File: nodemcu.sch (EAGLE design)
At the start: 6 parts

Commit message: uprava desky
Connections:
- new net N$6: U$1.VIN
- net +3V3: now also U$1.3V3@2; no longer U$1.VIN
- net GND: now also U$1.GND@3; no longer U$1.GND@1
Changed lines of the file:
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@@
 <?xml version="1.0" encoding="utf-8"?>
 <!DOCTYPE eagle SYSTEM "eagle.dtd">
-<eagle version="7.7.0">
+<eagle version="7.3.0">
 <drawing>
 <settings>
@@
 <segment>
 <pinref part="+3V1" gate="G$1" pin="+3V3"/>
-<pinref part="U$1" gate="G$1" pin="VIN"/>
 <wire x1="66.04" y1="43.18" x2="58.42" y2="43.18" width="0.1524" layer="91"/>
-<wire x1="7.62" y1="30.48" x2="5.08" y2="30.48" width="0.1524" layer="91"/>
-<wire x1="5.08" y1="30.48" x2="5.08" y2="17.78" width="0.1524" layer="91"/>
-<wire x1="5.08" y1="17.78" x2="15.24" y2="17.78" width="0.1524" layer="91"/>
 <wire x1="15.24" y1="17.78" x2="66.04" y2="17.78" width="0.1524" layer="91"/>
-<wire x1="66.04" y1="17.78" x2="66.04" y2="43.18" width="0.1524" layer="91"/>
+<wire x1="66.04" y1="17.78" x2="66.04" y2="30.48" width="0.1524" layer="91"/>
 <pinref part="SENSOR" gate="G$1" pin="1"/>
+<wire x1="66.04" y1="30.48" x2="66.04" y2="43.18" width="0.1524" layer="91"/>
 <wire x1="66.04" y1="43.18" x2="81.28" y2="43.18" width="0.1524" layer="91"/>
 <junction x="66.04" y="43.18"/>
 <pinref part="D1" gate="1" pin="C"/>
 <wire x1="15.24" y1="5.08" x2="15.24" y2="7.62" width="0.1524" layer="91"/>
-<junction x="15.24" y="17.78"/>
 <pinref part="SL2" gate="G$1" pin="1"/>
 <wire x1="15.24" y1="7.62" x2="15.24" y2="17.78" width="0.1524" layer="91"/>
@@
 <wire x1="22.86" y1="7.62" x2="22.86" y2="5.08" width="0.1524" layer="91"/>
 <junction x="15.24" y="7.62"/>
+<pinref part="U$1" gate="G$1" pin="3V3@2"/>
+<wire x1="43.18" y1="30.48" x2="66.04" y2="30.48" width="0.1524" layer="91"/>
+<junction x="66.04" y="30.48"/>
 </segment>
 </net>
@@
 <segment>
 <pinref part="GND1" gate="1" pin="GND"/>
-<wire x1="60.96" y1="27.94" x2="60.96" y2="40.64" width="0.1524" layer="91"/>
+<wire x1="60.96" y1="27.94" x2="60.96" y2="33.02" width="0.1524" layer="91"/>
 <pinref part="SENSOR" gate="G$1" pin="2"/>
+<wire x1="60.96" y1="33.02" x2="60.96" y2="40.64" width="0.1524" layer="91"/>
 <wire x1="60.96" y1="40.64" x2="81.28" y2="40.64" width="0.1524" layer="91"/>
 <wire x1="60.96" y1="27.94" x2="45.72" y2="27.94" width="0.1524" layer="91"/>
 <wire x1="45.72" y1="27.94" x2="45.72" y2="15.24" width="0.1524" layer="91"/>
 <junction x="60.96" y="27.94"/>
-<pinref part="U$1" gate="G$1" pin="GND@1"/>
-<wire x1="7.62" y1="33.02" x2="0" y2="33.02" width="0.1524" layer="91"/>
-<wire x1="0" y1="33.02" x2="0" y2="15.24" width="0.1524" layer="91"/>
 <pinref part="X1" gate="-1" pin="KL"/>
-<wire x1="0" y1="15.24" x2="10.16" y2="15.24" width="0.1524" layer="91"/>
 <wire x1="10.16" y1="15.24" x2="10.16" y2="-2.54" width="0.1524" layer="91"/>
 <wire x1="45.72" y1="15.24" x2="10.16" y2="15.24" width="0.1524" layer="91"/>
-<junction x="10.16" y="15.24"/>
+<pinref part="U$1" gate="G$1" pin="GND@3"/>
+<wire x1="43.18" y1="33.02" x2="60.96" y2="33.02" width="0.1524" layer="91"/>
+<junction x="60.96" y="33.02"/>
 </segment>
 </net>
@@
 </segment>
 </net>
+<net name="N$6" class="0">
+<segment>
+<pinref part="U$1" gate="G$1" pin="VIN"/>
+<wire x1="7.62" y1="30.48" x2="5.08" y2="30.48" width="0.1524" layer="91"/>
+</segment>
+</net>

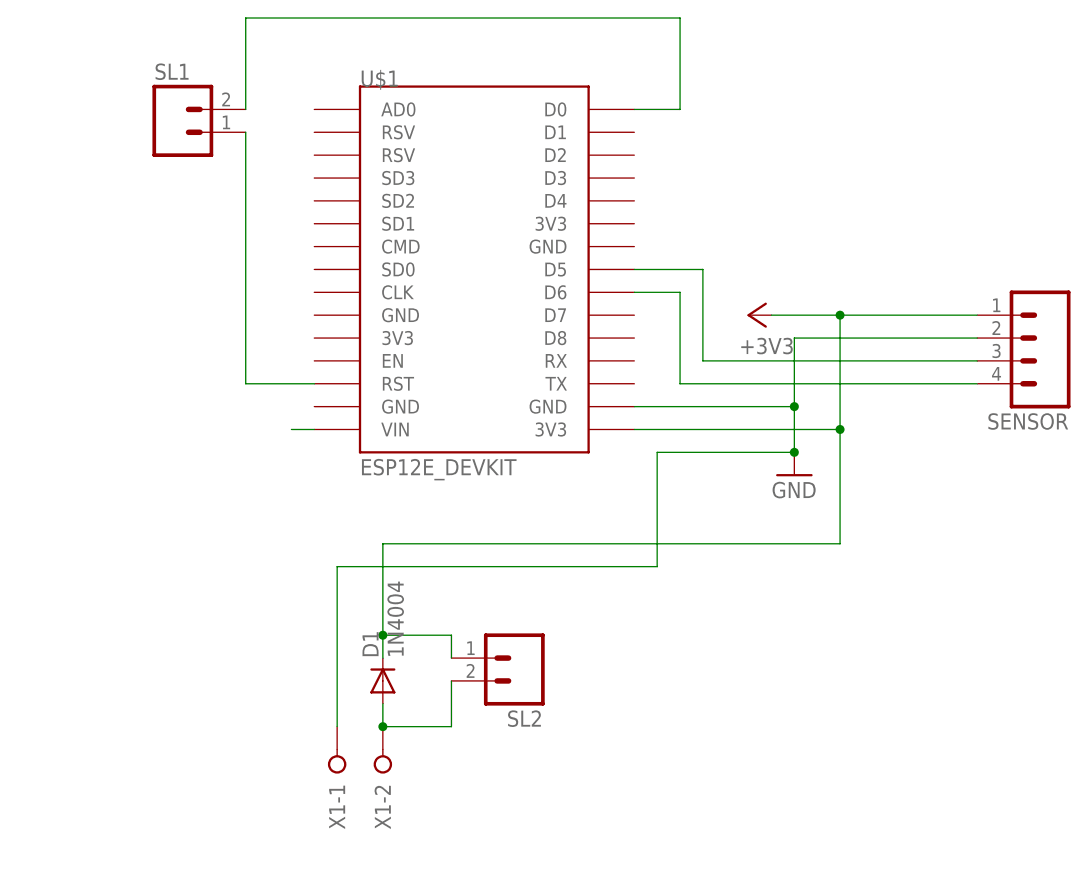
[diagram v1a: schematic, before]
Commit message: upraveno schema pro dip switch
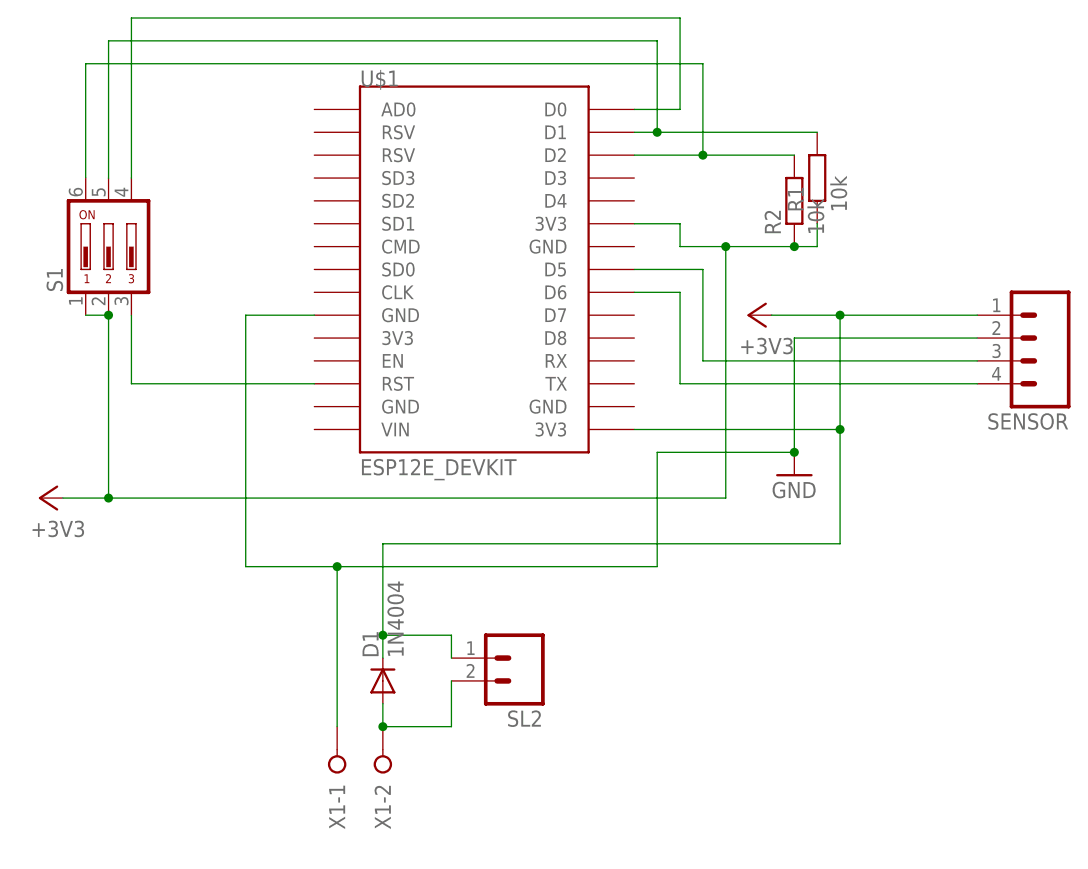
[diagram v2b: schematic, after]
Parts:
- removed SL1: (no value), con-amp-quick:M02
- added R1, R2: 10k, rcl:R-EU_0207/10
- added S1: (no value), switch-dil:DIP03YL
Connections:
- removed net N$6: U$1.VIN
- new net N$8: R1.2, S1.5, U$1.D1
- new net N$9: R2.2, S1.6, U$1.D2
- net +3V3: now also R1.1, R2.1, S1.1, S1.2, U$1.3V3@1
- net GND: now also U$1.GND@0; no longer U$1.GND@3
- net N$1: now also S1.4; no longer SL1.2
- net N$4: now also S1.3; no longer SL1.1
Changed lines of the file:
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@@
 <part name="GND1" library="supply1" deviceset="GND" device=""/>
 <part name="X1" library="con-wago-508" deviceset="W237-02P" device=""/>
-<part name="SL1" library="con-amp-quick" deviceset="M02" device=""/>
 <part name="D1" library="diode" deviceset="1N4004" device=""/>
 <part name="SL2" library="con-amp-quick" deviceset="M02" device=""/>
+<part name="S1" library="switch-dil" deviceset="DIP03YL" device=""/>
+<part name="R1" library="rcl" deviceset="R-EU_" device="0207/10" value="10k"/>
+<part name="R2" library="rcl" deviceset="R-EU_" device="0207/10" value="10k"/>
+<part name="+3V2" library="supply1" deviceset="+3V3" device=""/>
 </parts>
 <sheets>
@@
 <instance part="X1" gate="-1" x="10.16" y="-7.62" rot="R90"/>
 <instance part="X1" gate="-2" x="15.24" y="-7.62" rot="R90"/>
-<instance part="SL1" gate="G$1" x="-7.62" y="63.5"/>
 <instance part="D1" gate="1" x="15.24" y="2.54" rot="R90"/>
 <instance part="SL2" gate="G$1" x="30.48" y="5.08" rot="R180"/>
+<instance part="S1" gate="1" x="-15.24" y="50.8"/>
+<instance part="R1" gate="G$1" x="63.5" y="58.42" rot="R90"/>
+<instance part="R2" gate="G$1" x="60.96" y="55.88" rot="R90"/>
+<instance part="+3V2" gate="G$1" x="-22.86" y="22.86" rot="R90"/>
 </instances>
 <busses>
@@
 <junction x="66.04" y="30.48"/>
 </segment>
+<segment>
+<pinref part="S1" gate="1" pin="1"/>
+<pinref part="S1" gate="1" pin="2"/>
+<wire x1="-15.24" y1="43.18" x2="-17.78" y2="43.18" width="0.1524" layer="91"/>
+<wire x1="-15.24" y1="43.18" x2="-15.24" y2="22.86" width="0.1524" layer="91"/>
+<junction x="-15.24" y="43.18"/>
+<pinref part="R1" gate="G$1" pin="1"/>
+<wire x1="63.5" y1="50.8" x2="63.5" y2="53.34" width="0.1524" layer="91"/>
+<pinref part="R2" gate="G$1" pin="1"/>
+<wire x1="60.96" y1="50.8" x2="63.5" y2="50.8" width="0.1524" layer="91"/>
+<wire x1="60.96" y1="50.8" x2="53.34" y2="50.8" width="0.1524" layer="91"/>
+<wire x1="53.34" y1="50.8" x2="48.26" y2="50.8" width="0.1524" layer="91"/>
+<wire x1="48.26" y1="50.8" x2="48.26" y2="53.34" width="0.1524" layer="91"/>
+<junction x="60.96" y="50.8"/>
+<pinref part="U$1" gate="G$1" pin="3V3@1"/>
+<wire x1="48.26" y1="53.34" x2="43.18" y2="53.34" width="0.1524" layer="91"/>
+<wire x1="-15.24" y1="22.86" x2="53.34" y2="22.86" width="0.1524" layer="91"/>
+<wire x1="53.34" y1="22.86" x2="53.34" y2="50.8" width="0.1524" layer="91"/>
+<junction x="53.34" y="50.8"/>
+<pinref part="+3V2" gate="G$1" pin="+3V3"/>
+<wire x1="-20.32" y1="22.86" x2="-15.24" y2="22.86" width="0.1524" layer="91"/>
+<junction x="-15.24" y="22.86"/>
+</segment>
 </net>
 <net name="GND" class="0">
 <segment>
 <pinref part="GND1" gate="1" pin="GND"/>
-<wire x1="60.96" y1="27.94" x2="60.96" y2="33.02" width="0.1524" layer="91"/>
 <pinref part="SENSOR" gate="G$1" pin="2"/>
-<wire x1="60.96" y1="33.02" x2="60.96" y2="40.64" width="0.1524" layer="91"/>
+<wire x1="60.96" y1="27.94" x2="60.96" y2="40.64" width="0.1524" layer="91"/>
 <wire x1="60.96" y1="40.64" x2="81.28" y2="40.64" width="0.1524" layer="91"/>
 <wire x1="60.96" y1="27.94" x2="45.72" y2="27.94" width="0.1524" layer="91"/>
@@
 <wire x1="10.16" y1="15.24" x2="10.16" y2="-2.54" width="0.1524" layer="91"/>
 <wire x1="45.72" y1="15.24" x2="10.16" y2="15.24" width="0.1524" layer="91"/>
-<pinref part="U$1" gate="G$1" pin="GND@3"/>
-<wire x1="43.18" y1="33.02" x2="60.96" y2="33.02" width="0.1524" layer="91"/>
-<junction x="60.96" y="33.02"/>
+<pinref part="U$1" gate="G$1" pin="GND@0"/>
+<wire x1="7.62" y1="43.18" x2="0" y2="43.18" width="0.1524" layer="91"/>
+<wire x1="0" y1="43.18" x2="0" y2="15.24" width="0.1524" layer="91"/>
+<wire x1="0" y1="15.24" x2="10.16" y2="15.24" width="0.1524" layer="91"/>
+<junction x="10.16" y="15.24"/>
 </segment>
 </net>
 <net name="N$1" class="0">
 <segment>
-<wire x1="0" y1="66.04" x2="0" y2="76.2" width="0.1524" layer="91"/>
-<wire x1="0" y1="76.2" x2="48.26" y2="76.2" width="0.1524" layer="91"/>
+<wire x1="-12.7" y1="76.2" x2="48.26" y2="76.2" width="0.1524" layer="91"/>
 <wire x1="48.26" y1="76.2" x2="48.26" y2="66.04" width="0.1524" layer="91"/>
 <pinref part="U$1" gate="G$1" pin="D0"/>
 <wire x1="48.26" y1="66.04" x2="43.18" y2="66.04" width="0.1524" layer="91"/>
-<pinref part="SL1" gate="G$1" pin="2"/>
+<pinref part="S1" gate="1" pin="4"/>
+<wire x1="-12.7" y1="76.2" x2="-12.7" y2="58.42" width="0.1524" layer="91"/>
 </segment>
 </net>
@@
 <net name="N$4" class="0">
 <segment>
-<pinref part="SL1" gate="G$1" pin="1"/>
 <pinref part="U$1" gate="G$1" pin="RST"/>
-<wire x1="7.62" y1="35.56" x2="0" y2="35.56" width="0.1524" layer="91"/>
-<wire x1="0" y1="35.56" x2="0" y2="63.5" width="0.1524" layer="91"/>
+<pinref part="S1" gate="1" pin="3"/>
+<wire x1="-12.7" y1="43.18" x2="-12.7" y2="35.56" width="0.1524" layer="91"/>
+<wire x1="-12.7" y1="35.56" x2="7.62" y2="35.56" width="0.1524" layer="91"/>
 </segment>
 </net>
@@
 </segment>
 </net>
-<net name="N$6" class="0">
+<net name="N$8" class="0">
 <segment>
-<pinref part="U$1" gate="G$1" pin="VIN"/>
-<wire x1="7.62" y1="30.48" x2="5.08" y2="30.48" width="0.1524" layer="91"/>
+<pinref part="U$1" gate="G$1" pin="D1"/>
+<wire x1="43.18" y1="63.5" x2="45.72" y2="63.5" width="0.1524" layer="91"/>
+<wire x1="45.72" y1="63.5" x2="45.72" y2="73.66" width="0.1524" layer="91"/>
+<pinref part="S1" gate="1" pin="5"/>
+<wire x1="45.72" y1="73.66" x2="-15.24" y2="73.66" width="0.1524" layer="91"/>
+<wire x1="-15.24" y1="73.66" x2="-15.24" y2="58.42" width="0.1524" layer="91"/>
+<pinref part="R1" gate="G$1" pin="2"/>
+<wire x1="45.72" y1="63.5" x2="63.5" y2="63.5" width="0.1524" layer="91"/>
+<junction x="45.72" y="63.5"/>
 </segment>
 </net>
+<net name="N$9" class="0">
+<segment>
+<pinref part="U$1" gate="G$1" pin="D2"/>
+<wire x1="43.18" y1="60.96" x2="50.8" y2="60.96" width="0.1524" layer="91"/>
+<wire x1="50.8" y1="60.96" x2="50.8" y2="71.12" width="0.1524" layer="91"/>
+<pinref part="S1" gate="1" pin="6"/>
+<wire x1="50.8" y1="71.12" x2="-17.78" y2="71.12" width="0.1524" layer="91"/>
+<wire x1="-17.78" y1="71.12" x2="-17.78" y2="58.42" width="0.1524" layer="91"/>
+<pinref part="R2" gate="G$1" pin="2"/>
+<wire x1="50.8" y1="60.96" x2="60.96" y2="60.96" width="0.1524" layer="91"/>
+<junction x="50.8" y="60.96"/>
+</segment>
+</net>

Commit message: upravy spoje
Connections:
- net +3V3: no longer S1.1, S1.2
- net GND: now also S1.1, S1.2
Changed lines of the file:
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@@
 <?xml version="1.0" encoding="utf-8"?>
 <!DOCTYPE eagle SYSTEM "eagle.dtd">
-<eagle version="7.3.0">
+<eagle version="7.7.0">
 <drawing>
 <settings>
@@
 <part name="R1" library="rcl" deviceset="R-EU_" device="0207/10" value="10k"/>
 <part name="R2" library="rcl" deviceset="R-EU_" device="0207/10" value="10k"/>
-<part name="+3V2" library="supply1" deviceset="+3V3" device=""/>
 </parts>
 <sheets>
@@
 <instance part="R1" gate="G$1" x="63.5" y="58.42" rot="R90"/>
 <instance part="R2" gate="G$1" x="60.96" y="55.88" rot="R90"/>
-<instance part="+3V2" gate="G$1" x="-22.86" y="22.86" rot="R90"/>
 </instances>
 <busses>
@@
 <segment>
 <pinref part="+3V1" gate="G$1" pin="+3V3"/>
-<wire x1="66.04" y1="43.18" x2="58.42" y2="43.18" width="0.1524" layer="91"/>
+<wire x1="66.04" y1="43.18" x2="60.96" y2="43.18" width="0.1524" layer="91"/>
+<wire x1="60.96" y1="43.18" x2="58.42" y2="43.18" width="0.1524" layer="91"/>
 <wire x1="15.24" y1="17.78" x2="66.04" y2="17.78" width="0.1524" layer="91"/>
 <wire x1="66.04" y1="17.78" x2="66.04" y2="30.48" width="0.1524" layer="91"/>
@@
 <wire x1="43.18" y1="30.48" x2="66.04" y2="30.48" width="0.1524" layer="91"/>
 <junction x="66.04" y="30.48"/>
-</segment>
-<segment>
-<pinref part="S1" gate="1" pin="1"/>
-<pinref part="S1" gate="1" pin="2"/>
-<wire x1="-15.24" y1="43.18" x2="-17.78" y2="43.18" width="0.1524" layer="91"/>
-<wire x1="-15.24" y1="43.18" x2="-15.24" y2="22.86" width="0.1524" layer="91"/>
-<junction x="-15.24" y="43.18"/>
 <pinref part="R1" gate="G$1" pin="1"/>
 <wire x1="63.5" y1="50.8" x2="63.5" y2="53.34" width="0.1524" layer="91"/>
 <pinref part="R2" gate="G$1" pin="1"/>
 <wire x1="60.96" y1="50.8" x2="63.5" y2="50.8" width="0.1524" layer="91"/>
-<wire x1="60.96" y1="50.8" x2="53.34" y2="50.8" width="0.1524" layer="91"/>
-<wire x1="53.34" y1="50.8" x2="48.26" y2="50.8" width="0.1524" layer="91"/>
-<wire x1="48.26" y1="50.8" x2="48.26" y2="53.34" width="0.1524" layer="91"/>
 <junction x="60.96" y="50.8"/>
+<wire x1="60.96" y1="50.8" x2="60.96" y2="43.18" width="0.1524" layer="91"/>
+<junction x="60.96" y="43.18"/>
 <pinref part="U$1" gate="G$1" pin="3V3@1"/>
-<wire x1="48.26" y1="53.34" x2="43.18" y2="53.34" width="0.1524" layer="91"/>
-<wire x1="-15.24" y1="22.86" x2="53.34" y2="22.86" width="0.1524" layer="91"/>
-<wire x1="53.34" y1="22.86" x2="53.34" y2="50.8" width="0.1524" layer="91"/>
-<junction x="53.34" y="50.8"/>
-<pinref part="+3V2" gate="G$1" pin="+3V3"/>
-<wire x1="-20.32" y1="22.86" x2="-15.24" y2="22.86" width="0.1524" layer="91"/>
-<junction x="-15.24" y="22.86"/>
+<wire x1="43.18" y1="53.34" x2="53.34" y2="53.34" width="0.1524" layer="91"/>
+<wire x1="53.34" y1="53.34" x2="53.34" y2="50.8" width="0.1524" layer="91"/>
+<wire x1="53.34" y1="50.8" x2="60.96" y2="50.8" width="0.1524" layer="91"/>
 </segment>
 </net>
@@
 <wire x1="0" y1="15.24" x2="10.16" y2="15.24" width="0.1524" layer="91"/>
 <junction x="10.16" y="15.24"/>
+<pinref part="S1" gate="1" pin="1"/>
+<pinref part="S1" gate="1" pin="2"/>
+<wire x1="-15.24" y1="43.18" x2="-17.78" y2="43.18" width="0.1524" layer="91"/>
+<wire x1="-17.78" y1="43.18" x2="-17.78" y2="15.24" width="0.1524" layer="91"/>
+<junction x="-17.78" y="43.18"/>
+<wire x1="-17.78" y1="15.24" x2="0" y2="15.24" width="0.1524" layer="91"/>
+<junction x="0" y="15.24"/>
 </segment>
 </net>
